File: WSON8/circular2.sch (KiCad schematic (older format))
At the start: 34 parts, among them J101 Conn_Coaxial, J102 Conn_01x03, U101 LT3042xMSE, U102 LT3093xMSE, U103 OPA859xDSG

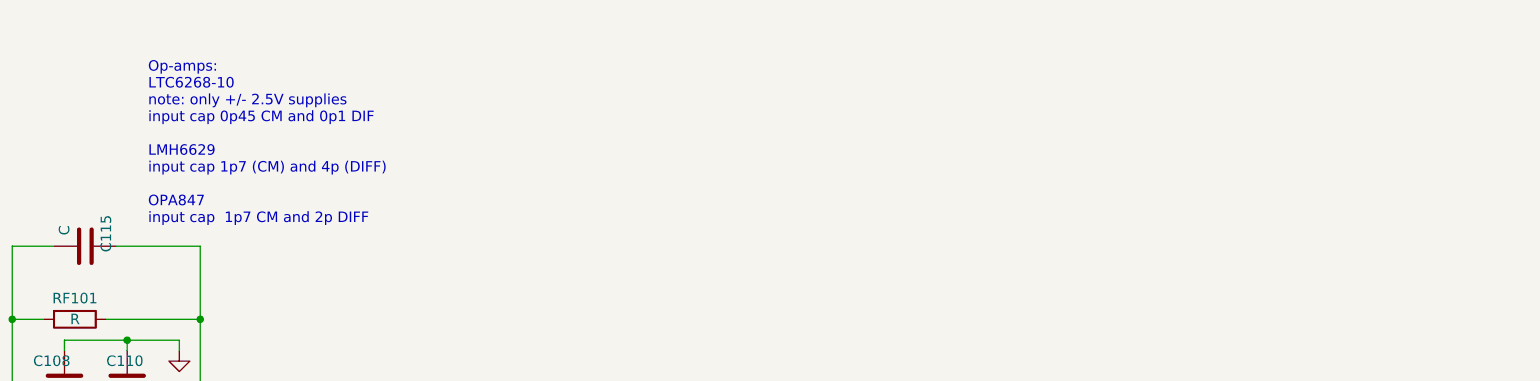
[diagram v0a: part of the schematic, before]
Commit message: add ohwr-texts to wson8 files
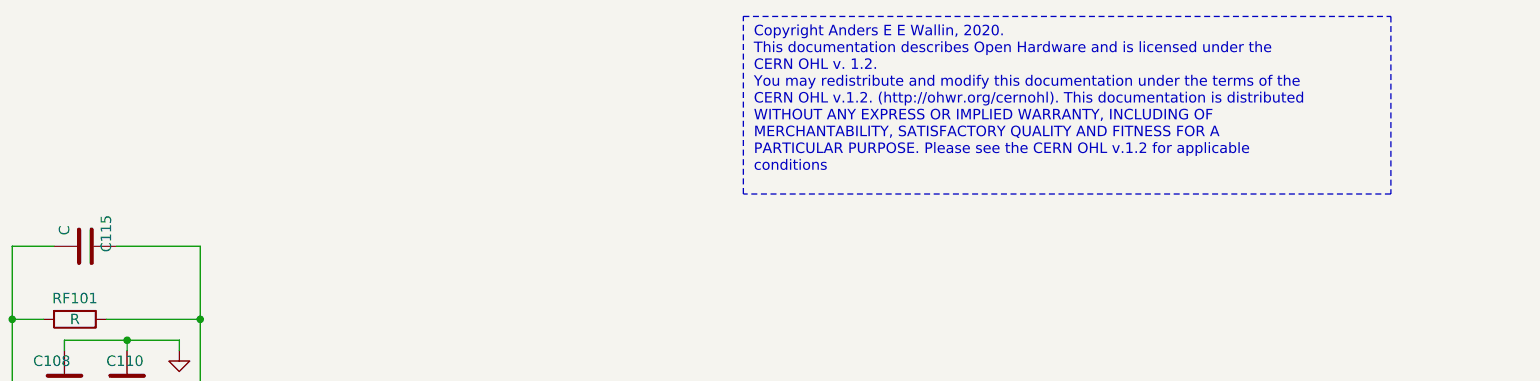
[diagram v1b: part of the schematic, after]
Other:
- note added: "Copyright Anders E E Wallin, 2020.\nThis documentation describes Open Hardware and is licensed under the\nCERN OHL v. 1.2.\nYou may redistribute and modify this documentation under the terms of the\nCERN OHL v.1.2. (http://ohwr.org/cernohl). This documentation is distributed\nWITHOUT ANY EXPRESS OR IMPLIED WARRANTY, INCLUDING OF\nMERCHANTABILITY, SATISFACTORY QUALITY AND FITNESS FOR A\nPARTICULAR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"
- note removed: "Op-amps:\nLTC6268-10\nnote: only +/- 2.5V supplies\ninput cap 0p45 CM and 0p1 DIF \n\nLMH6629\ninput cap 1p7 (CM) and 4p (DIFF)\n\nOPA847\ninput cap 1p7 CM and 2p DIFF"
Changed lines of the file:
@@
 encoding utf-8
 Sheet 1 1
-Title "1\" Photodiode Transimpedance Amplifier"
+Title "1\" Photodiode Transimpedance Amplifier - WSON8"
 Date "2019-12-20"
 Rev "draft"
@@
 Text Notes 10250 6400 0    50   ~ 0
 Open Hardware
-Text Notes 5000 1750 0    50   ~ 0
-Op-amps:\nLTC6268-10\nnote: only +/- 2.5V supplies\ninput cap 0p45 CM and 0p1 DIF \n\nLMH6629\ninput cap 1p7 (CM) and 4p (DIFF)\n\nOPA847\ninput cap  1p7 CM and 2p DIFF
 Text Notes 1100 2400 0    50   ~ 0
 Alternative photodiodes\nOSI FCI-125G-006HRL\nHamamatsu S9055(-01)\nThorlabs FDS015, FDS025
@@
 Text Label 2750 6300 0    50   ~ 0
 SET-
+Text Notes 7900 1500 0    50   ~ 0
+Copyright Anders E E Wallin, 2020.\nThis documentation describes Open Hardware and is licensed under the\nCERN OHL v. 1.2.\nYou may redistribute and modify this documentation under the terms of the\nCERN OHL v.1.2. (http://ohwr.org/cernohl). This documentation is distributed\nWITHOUT ANY EXPRESS OR IMPLIED WARRANTY, INCLUDING OF\nMERCHANTABILITY, SATISFACTORY QUALITY AND FITNESS FOR A\nPARTICULAR PURPOSE. Please see the CERN OHL v.1.2 for applicable\nconditions\n
+Wire Notes Line
+	7850 750  10950 750
+Wire Notes Line
+	10950 750  10950 1600
+Wire Notes Line
+	10950 1600 7850 1600
+Wire Notes Line
+	7850 1600 7850 750
 $EndSCHEMATC

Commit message: component values
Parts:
- C102, C110, C111: value C -> 4u7
- C104: value C -> 10n
- C108, C109: value C -> 100n
- R101, R107: value 49k9 -> 25k
- R103: value R -> 0R
- R106: value R -> 49R9
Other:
- note added: "FET opamp\nR104 = 0 R\nomit C105, C106"
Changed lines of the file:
@@
 U 1 1 5E080F1F
 P 3750 2550
-F 0 "R103" V 3543 2550 50  0000 C CNN
-F 1 "R" V 3634 2550 50  0000 C CNN
+F 0 "R103" V 3650 2550 50  0000 C CNN
+F 1 "0R" V 3750 2550 50  0000 C CNN
 F 2 "Resistor_SMD:R_0603_1608Metric" V 3680 2550 50  0001 C CNN
 F 3 "~" H 3750 2550 50  0001 C CNN
@@
 U 1 1 5E0831FD
 P 5700 3050
-F 0 "R106" V 5493 3050 50  0000 C CNN
-F 1 "R" V 5584 3050 50  0000 C CNN
+F 0 "R106" V 5600 3050 50  0000 C CNN
+F 1 "49R9" V 5700 3050 50  0000 C CNN
 F 2 "Resistor_SMD:R_0603_1608Metric" V 5630 3050 50  0001 C CNN
 F 3 "~" H 5700 3050 50  0001 C CNN
@@
 P 4600 3600
 F 0 "C109" H 4400 3700 50  0000 L CNN
-F 1 "C" H 4500 3500 50  0000 L CNN
+F 1 "100n" H 4400 3500 50  0000 L CNN
 F 2 "Capacitor_SMD:C_0603_1608Metric" H 4638 3450 50  0001 C CNN
 F 3 "~" H 4600 3600 50  0001 C CNN
@@
 P 4900 3600
 F 0 "C111" H 5015 3646 50  0000 L CNN
-F 1 "C" H 5015 3555 50  0000 L CNN
+F 1 "4u7" H 5050 3550 50  0000 L CNN
 F 2 "Capacitor_SMD:C_0603_1608Metric" H 4938 3450 50  0001 C CNN
 F 3 "~" H 4900 3600 50  0001 C CNN
@@
 P 4600 2500
 F 0 "C108" H 4450 2600 50  0000 L CNN
-F 1 "C" H 4550 2400 50  0000 L CNN
+F 1 "100n" H 4550 2400 50  0000 L CNN
 F 2 "Capacitor_SMD:C_0603_1608Metric" H 4638 2350 50  0001 C CNN
 F 3 "~" H 4600 2500 50  0001 C CNN
@@
 P 4900 2500
 F 0 "C110" H 4800 2600 50  0000 L CNN
-F 1 "C" H 4850 2400 50  0000 L CNN
+F 1 "4u7" H 4850 2400 50  0000 L CNN
 F 2 "Capacitor_SMD:C_0603_1608Metric" H 4938 2350 50  0001 C CNN
 F 3 "~" H 4900 2500 50  0001 C CNN
@@
 P 2750 2250
 F 0 "C104" H 2865 2296 50  0000 L CNN
-F 1 "C" H 2865 2205 50  0000 L CNN
+F 1 "10n" H 2865 2205 50  0000 L CNN
 F 2 "Capacitor_SMD:C_0603_1608Metric" H 2788 2100 50  0001 C CNN
 F 3 "~" H 2750 2250 50  0001 C CNN
@@
 P 2400 2250
 F 0 "C102" H 2515 2296 50  0000 L CNN
-F 1 "C" H 2515 2205 50  0000 L CNN
+F 1 "4u7" H 2515 2205 50  0000 L CNN
 F 2 "Capacitor_SMD:C_0603_1608Metric" H 2438 2100 50  0001 C CNN
 F 3 "~" H 2400 2250 50  0001 C CNN
@@
 P 2900 5250
 F 0 "R101" H 2970 5296 50  0000 L CNN
-F 1 "49k9" H 2970 5205 50  0000 L CNN
+F 1 "25k" H 2970 5205 50  0000 L CNN
 F 2 "Resistor_SMD:R_0603_1608Metric" V 2830 5250 50  0001 C CNN
 F 3 "~" H 2900 5250 50  0001 C CNN
@@
 P 2950 6100
 F 0 "R107" H 3020 6146 50  0000 L CNN
-F 1 "49k9" H 3020 6055 50  0000 L CNN
+F 1 "25k" H 3020 6055 50  0000 L CNN
 F 2 "Resistor_SMD:R_0603_1608Metric" V 2880 6100 50  0001 C CNN
 F 3 "~" H 2950 6100 50  0001 C CNN
@@
 Wire Wire Line
 	4200 6700 4450 6700
-Text Notes 5050 3200 0    50   ~ 0
+Text Notes 4700 3300 0    50   ~ 0
 296-46172-1-ND
 Text Notes 2150 3000 0    50   ~ 0
@@
 U 1 1 5E31BB57
 P 4700 3050
-F 0 "U103" H 4700 2661 50  0000 C CNN
-F 1 "OPA859xDSG" H 4700 2570 50  0000 C CNN
+F 0 "U103" H 4950 3000 50  0000 C CNN
+F 1 "OPA859xDSG" H 5000 2900 50  0000 C CNN
 F 2 "Package_SON:WSON-8-1EP_2x2mm_P0.5mm_EP0.9x1.6mm" H 4600 3650 50  0001 C CNN
 F 3 "http://www.ti.com/lit/ds/symlink/opa859.pdf" H 5100 3450 50  0001 C CNN
@@
 Wire Notes Line
 	7850 1600 7850 750
+Text Notes 3700 3850 0    50   ~ 0
+FET opamp\nR104 = 0 R\nomit C105, C106
 $EndSCHEMATC

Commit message: update docs
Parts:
- D102: symbol circular2-rescue:S597x-aw-circulaire-rescue -> Sensor_Optical:S5973
- U102: symbol circular2-rescue:LT3093xMSE-aw-circulaire-rescue -> Regulator_Linear:LT3093xMSE
- U103: symbol circular2-rescue:OPA859xDSG-Amplifier_Operational -> Amplifier_Operational:OPA859xDSG
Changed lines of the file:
@@
 $EndDescr
 $Comp
-L circular2-rescue:S597x-aw-circulaire-rescue D102
+L Sensor_Optical:S5973 D102
 U 1 1 5E080605
 P 3250 2550
@@
 $EndComp
 $Comp
-L circular2-rescue:LT3093xMSE-aw-circulaire-rescue U102
+L Regulator_Linear:LT3093xMSE U102
 U 1 1 5DFD4B04
-P 3400 6600
-F 0 "U102" H 3400 6875 50  0000 C CNN
-F 1 "LT3093xMSE" H 3400 6966 50  0000 C CNN
-F 2 "Package_SO:MSOP-12-1EP_3x4mm_P0.65mm_EP1.65x2.85mm" H 3400 6925 50  0001 C CNN
-F 3 "" H 3400 6600 50  0001 C CNN
-	1    3400 6600
+P 3400 6500
+F 0 "U102" H 3400 6775 50  0000 C CNN
+F 1 "LT3093xMSE" H 3400 6866 50  0000 C CNN
+F 2 "Package_SO:MSOP-12-1EP_3x4mm_P0.65mm_EP1.65x2.85mm" H 3400 6825 50  0001 C CNN
+F 3 "" H 3400 6500 50  0001 C CNN
+	1    3400 6500
 	1    0    0    1
 $EndComp
@@
 Connection ~ 4350 2200
 $Comp
-L circular2-rescue:OPA859xDSG-Amplifier_Operational U103
+L Amplifier_Operational:OPA859xDSG U103
 U 1 1 5E31BB57
 P 4700 3050
